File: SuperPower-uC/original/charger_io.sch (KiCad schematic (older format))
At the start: 21 parts, among them J2 Barrel_Jack_Switch, J3 Conn_01x02_Male, Q2 DMP3028LSD, U2 USB-C, U3 IP4220CZ6

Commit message: Update Placement + Increase MTG Hole Size
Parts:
- H1, H3: footprint MountingHole:MountingHole_2.2mm_M2_Pad_Via -> MountingHole:MountingHole_2.7mm_M2.5_Pad_Via
- H2, H4: footprint MountingHole:MountingHole_2.2mm_M2_Pad_Via -> MountingHole:MountingHole_2.7mm_Pad_Via
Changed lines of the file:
@@
 F 0 "H1" H 1450 2599 50  0000 L CNN
 F 1 "MountingHole_Pad" H 1450 2508 50  0000 L CNN
-F 2 "MountingHole:MountingHole_2.2mm_M2_Pad_Via" H 1350 2550 50  0001 C CNN
+F 2 "MountingHole:MountingHole_2.7mm_M2.5_Pad_Via" H 1350 2550 50  0001 C CNN
 F 3 "~" H 1350 2550 50  0001 C CNN
 	1    1350 2550
@@
 F 0 "H3" H 2350 2599 50  0000 L CNN
 F 1 "MountingHole_Pad" H 2350 2508 50  0000 L CNN
-F 2 "MountingHole:MountingHole_2.2mm_M2_Pad_Via" H 2250 2550 50  0001 C CNN
+F 2 "MountingHole:MountingHole_2.7mm_M2.5_Pad_Via" H 2250 2550 50  0001 C CNN
 F 3 "~" H 2250 2550 50  0001 C CNN
 	1    2250 2550
@@
 F 0 "H2" H 1450 3349 50  0000 L CNN
 F 1 "MountingHole_Pad" H 1450 3258 50  0000 L CNN
-F 2 "MountingHole:MountingHole_2.2mm_M2_Pad_Via" H 1350 3300 50  0001 C CNN
+F 2 "MountingHole:MountingHole_2.7mm_Pad_Via" H 1350 3300 50  0001 C CNN
 F 3 "~" H 1350 3300 50  0001 C CNN
 	1    1350 3300
@@
 F 0 "H4" H 2350 3349 50  0000 L CNN
 F 1 "MountingHole_Pad" H 2350 3258 50  0000 L CNN
-F 2 "MountingHole:MountingHole_2.2mm_M2_Pad_Via" H 2250 3300 50  0001 C CNN
+F 2 "MountingHole:MountingHole_2.7mm_Pad_Via" H 2250 3300 50  0001 C CNN
 F 3 "~" H 2250 3300 50  0001 C CNN
 	1    2250 3300

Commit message: Update DC Power Jack connector
Add 3D Model
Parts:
- J2: footprint Connector_BarrelJack:BarrelJack_CUI_PJ-102AH_Horizontal -> Connector_BarrelJack:BarrelJack_Wuerth_6941xx301002
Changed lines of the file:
@@
 F 0 "J2" H 4257 3317 50  0000 C CNN
 F 1 "Barrel_Jack_Switch" H 4257 3226 50  0000 C CNN
-F 2 "Connector_BarrelJack:BarrelJack_CUI_PJ-102AH_Horizontal" H 4250 2960 50  0001 C CNN
+F 2 "Connector_BarrelJack:BarrelJack_Wuerth_6941xx301002" H 4250 2960 50  0001 C CNN
 F 3 "~" H 4250 2960 50  0001 C CNN
 	1    4200 3000

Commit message: Update DMP3028LSD SO-8 3D Package
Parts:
- Q2: footprint Package_SO:SO-8_3.9x4.9mm_P1.27mm -> DMP3028LSD:SO-8_3.9x4.9mm_P1.27mm
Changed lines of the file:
@@
 F 0 "Q2" V 10057 3075 50  0000 C CNN
 F 1 "DMP3028LSD" V 9966 3075 50  0000 C CNN
-F 2 "Package_SO:SO-8_3.9x4.9mm_P1.27mm" H 9700 2975 50  0001 L CIN
+F 2 "DMP3028LSD:SO-8_3.9x4.9mm_P1.27mm" H 9700 2975 50  0001 L CIN
 F 3 "https://www.diodes.com/assets/Datasheets/DMP3028LSD.pdf" V 9500 3050 50  0001 L CNN
 F 4 "Diodes Incorporated" H 9500 3050 50  0001 C CNN "Mfr_name"

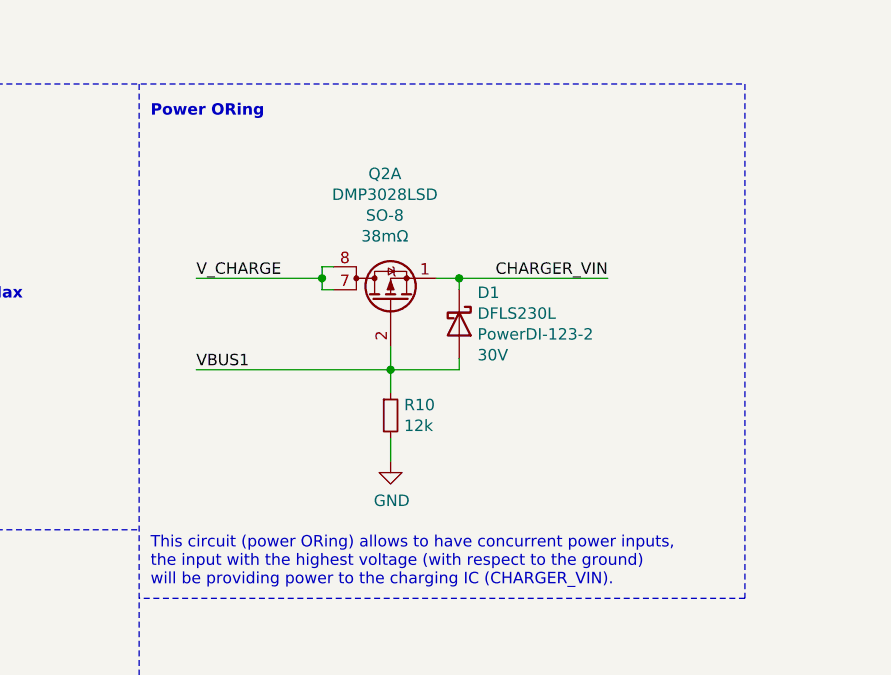
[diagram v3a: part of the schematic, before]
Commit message: Add a second optional Schottky diode for High Current
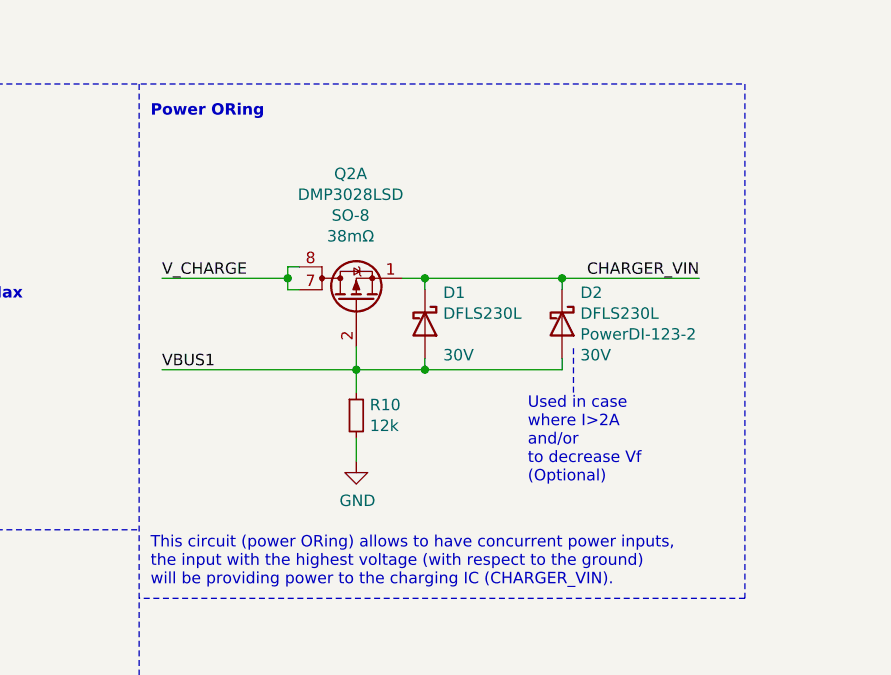
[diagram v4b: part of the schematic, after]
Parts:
- added D2: DFLS230L, Diode_SMD:D_PowerDI-123, symbol dfls230l:DFLS230L
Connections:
- net CHARGER_VIN: now also D2.1 (K)
- net VBUS1: now also D2.2 (A)
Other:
- note added: "Used in case \nwhere I>2A\nand/or\nto decrease Vf\n(Optional)"
- moved on the sheet: D1, Q2A, R10

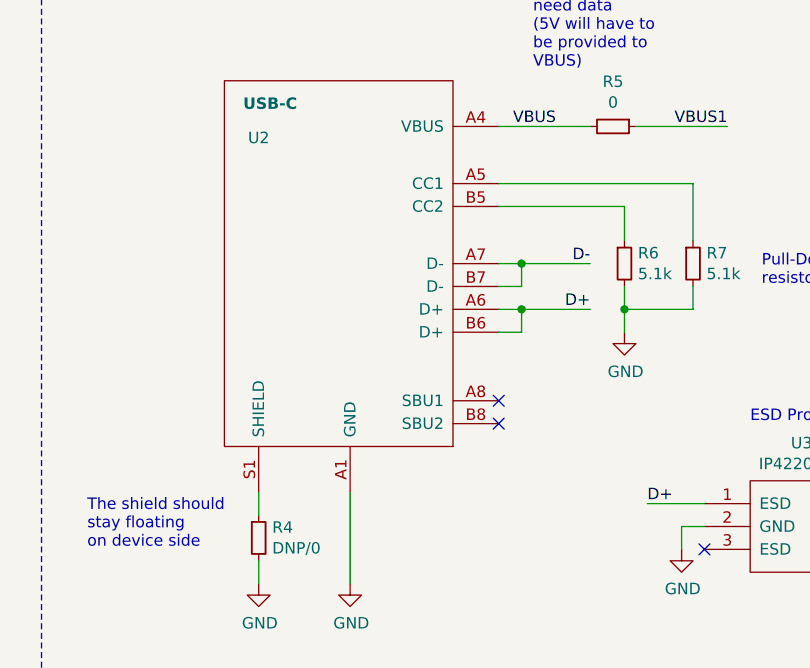
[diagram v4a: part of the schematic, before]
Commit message: Update Placement USB_UART_Bridge
+ Misc.
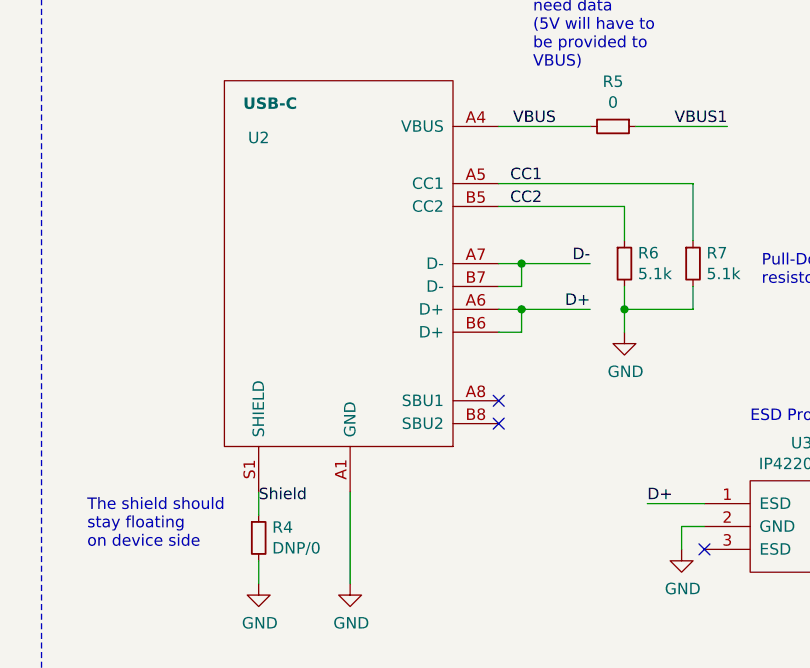
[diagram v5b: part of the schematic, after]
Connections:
- net CC2: now reaches R6.1, U2.B5 (CC2)
- net CC1: now reaches R7.1, U2.A5 (CC1)
- net Shield: now reaches R4.1, U2.S1 (SHIELD)
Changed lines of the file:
@@
 Wire Notes Line
 	10300 3450 10300 3250
+Text Label 3150 5300 0    50   ~ 0
+CC1
+Text Label 3150 5400 0    50   ~ 0
+CC2
+Text Label 2050 6700 0    50   ~ 0
+Shield
 $EndSCHEMATC
